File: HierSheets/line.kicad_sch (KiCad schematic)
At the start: 72 parts, among them Q10 SFH309, Q11 SFH309, Q12 SFH309, Q17 SFH309, Q18 SFH309, Q19 SFH309, Q20 SFH309, Q21 SFH309, Q22 SFH309, Q23 SFH309, Q24 SFH309, Q25 SFH309, Q26 SFH309, Q27 SFH309, Q28 SFH309, Q9 SFH309, U13 ADS1115IDGS, U14 ADS1115IDGS, U15 ADS1115IDGS, U16 ADS1115IDGS

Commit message: aaa
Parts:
- removed C11, C12: C0.1uF, symbol Device:C
- removed D21, D22, D23, D24, D25, D26, D27, D28: SFH_4656-Z, symbol Device:LED
- removed Q21, Q22, Q23, Q24, Q25, Q26, Q27, Q28: SFH309, LED_THT:LED_D3.0mm_Clear, symbol Sensor_Optical:SFH309
- removed R62, R63, R64, R65, R70, R71, R72, R73: 750R, symbol Device:R
- removed R66, R67, R68, R69, R74, R75, R76, R77: 10kR, symbol Device:R
- removed U15, U16: ADS1115IDGS, Package_SO:TSSOP-10_3x3mm_P0.5mm, symbol Analog_ADC:ADS1115IDGS

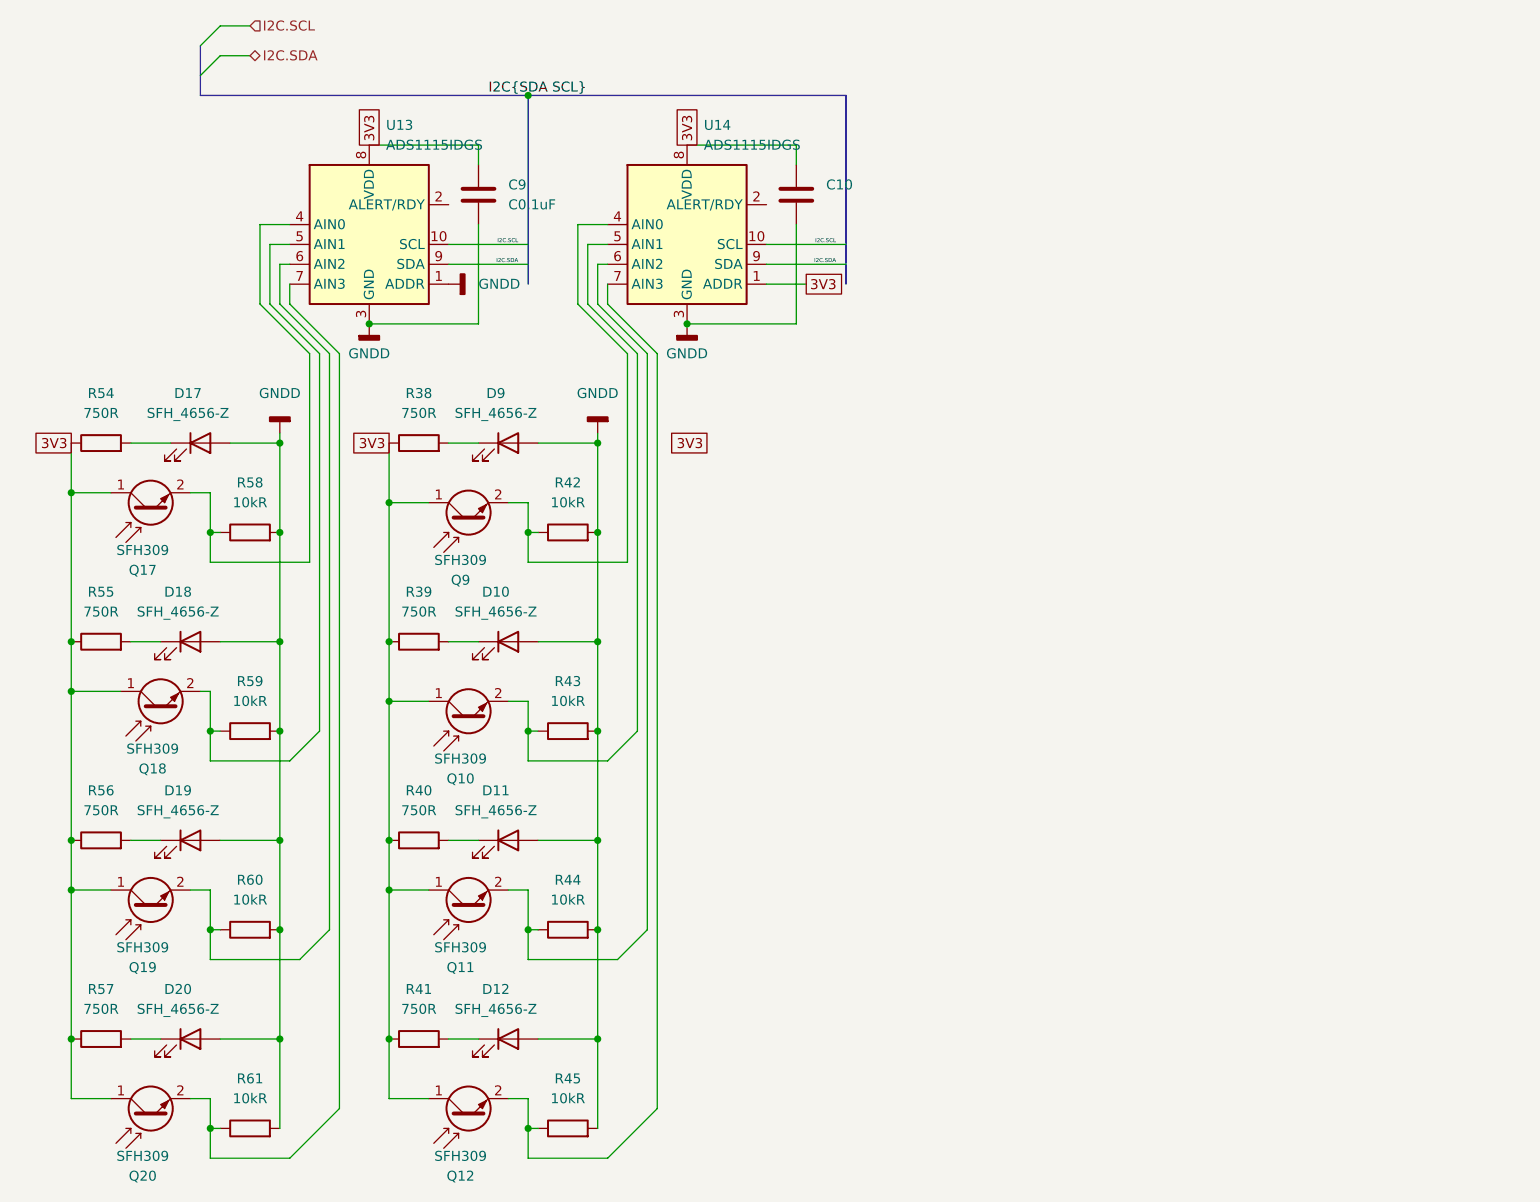
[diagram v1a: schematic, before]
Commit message: Added kicker, interrupt, I2C pullups, buck converter, button
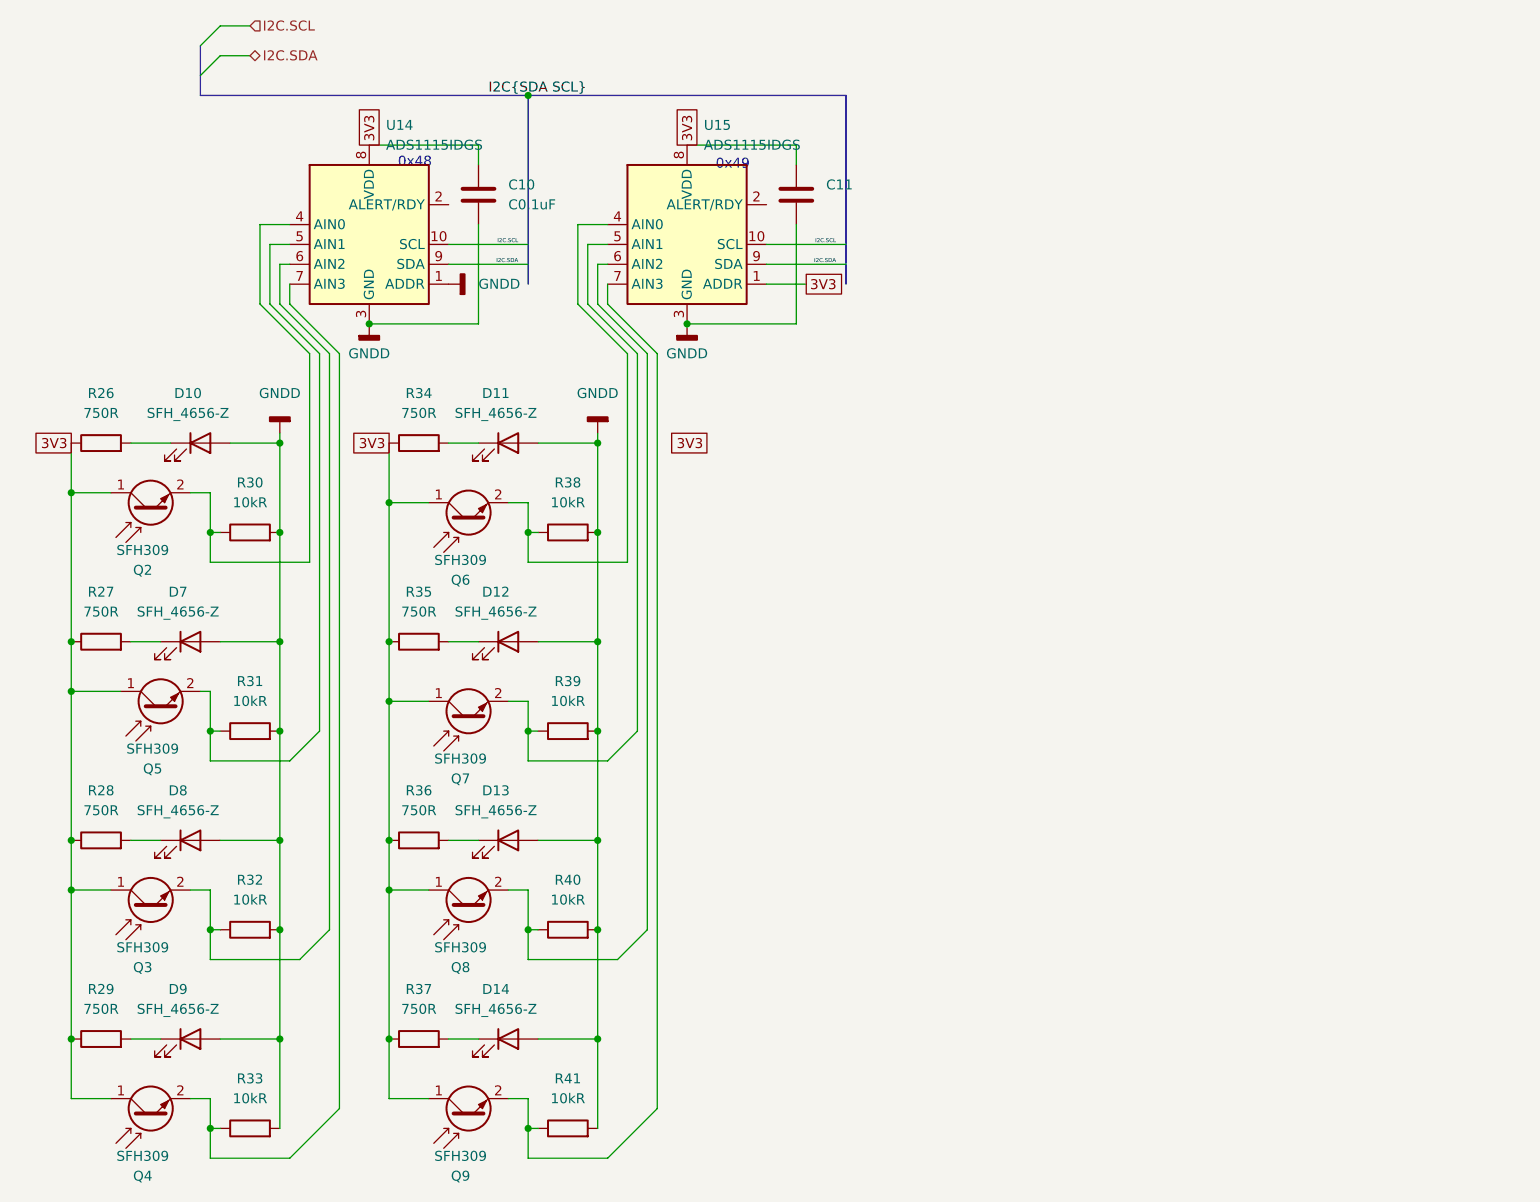
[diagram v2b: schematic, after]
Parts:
- renumbered C9 to C10, C10 to C11, D17 to D10, D9 to D11, D10 to D12, D11 to D13, D12 to D14, D18 to D7, D19 to D8, D20 to D9, Q17 to Q2, Q19 to Q3, Q20 to Q4, Q18 to Q5, Q9 to Q6, Q10 to Q7, Q11 to Q8, Q12 to Q9, R54 to R26, R55 to R27, R56 to R28, R57 to R29, R58 to R30, R59 to R31, R60 to R32, R61 to R33, R38 to R34, R39 to R35, R40 to R36, R41 to R37, R42 to R38, R43 to R39, R44 to R40, R45 to R41, U13 to U14, U14 to U15
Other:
- note added: "0x48"
- note added: "0x49"
